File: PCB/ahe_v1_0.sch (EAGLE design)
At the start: 19 parts, among them CN1 1X4-BIG, CN3 1X4SMT, IC1 MS560702BA03-50, IC2 MCP73871-1CCI_ML, IC3 TPS7A2055PDBVR, J1 USB3075-30-A

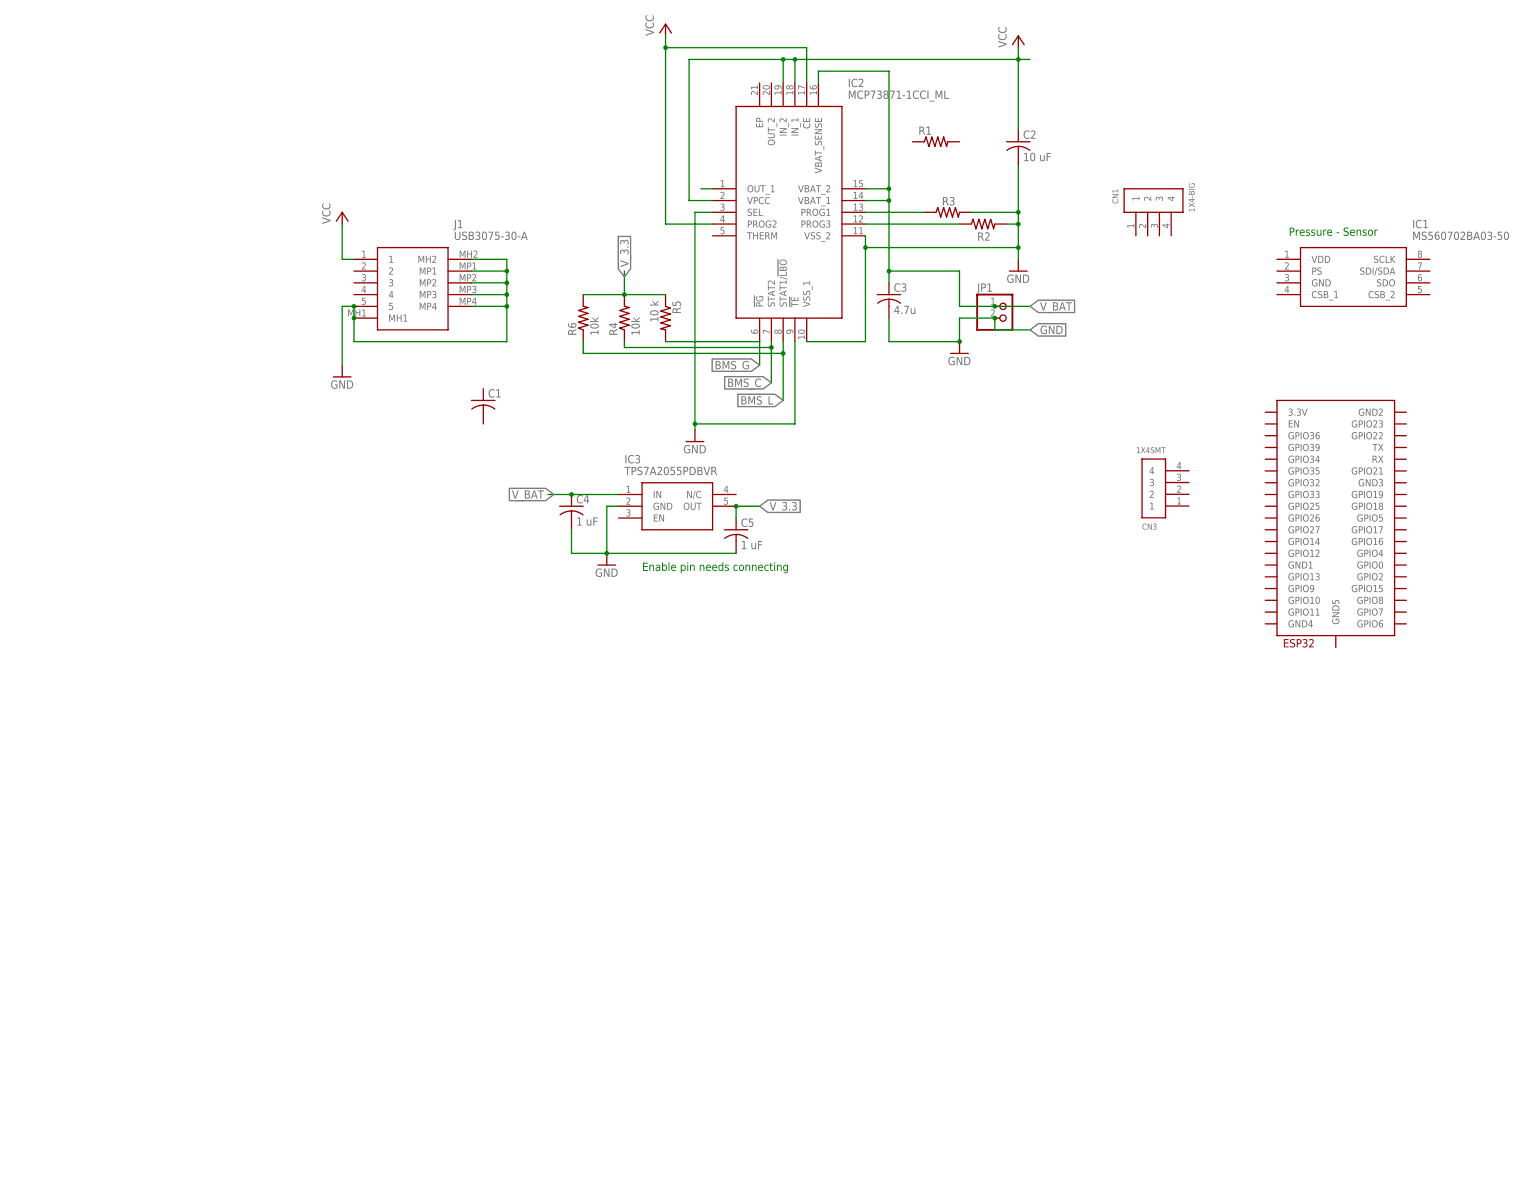
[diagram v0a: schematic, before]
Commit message: Completed BMS/LDO
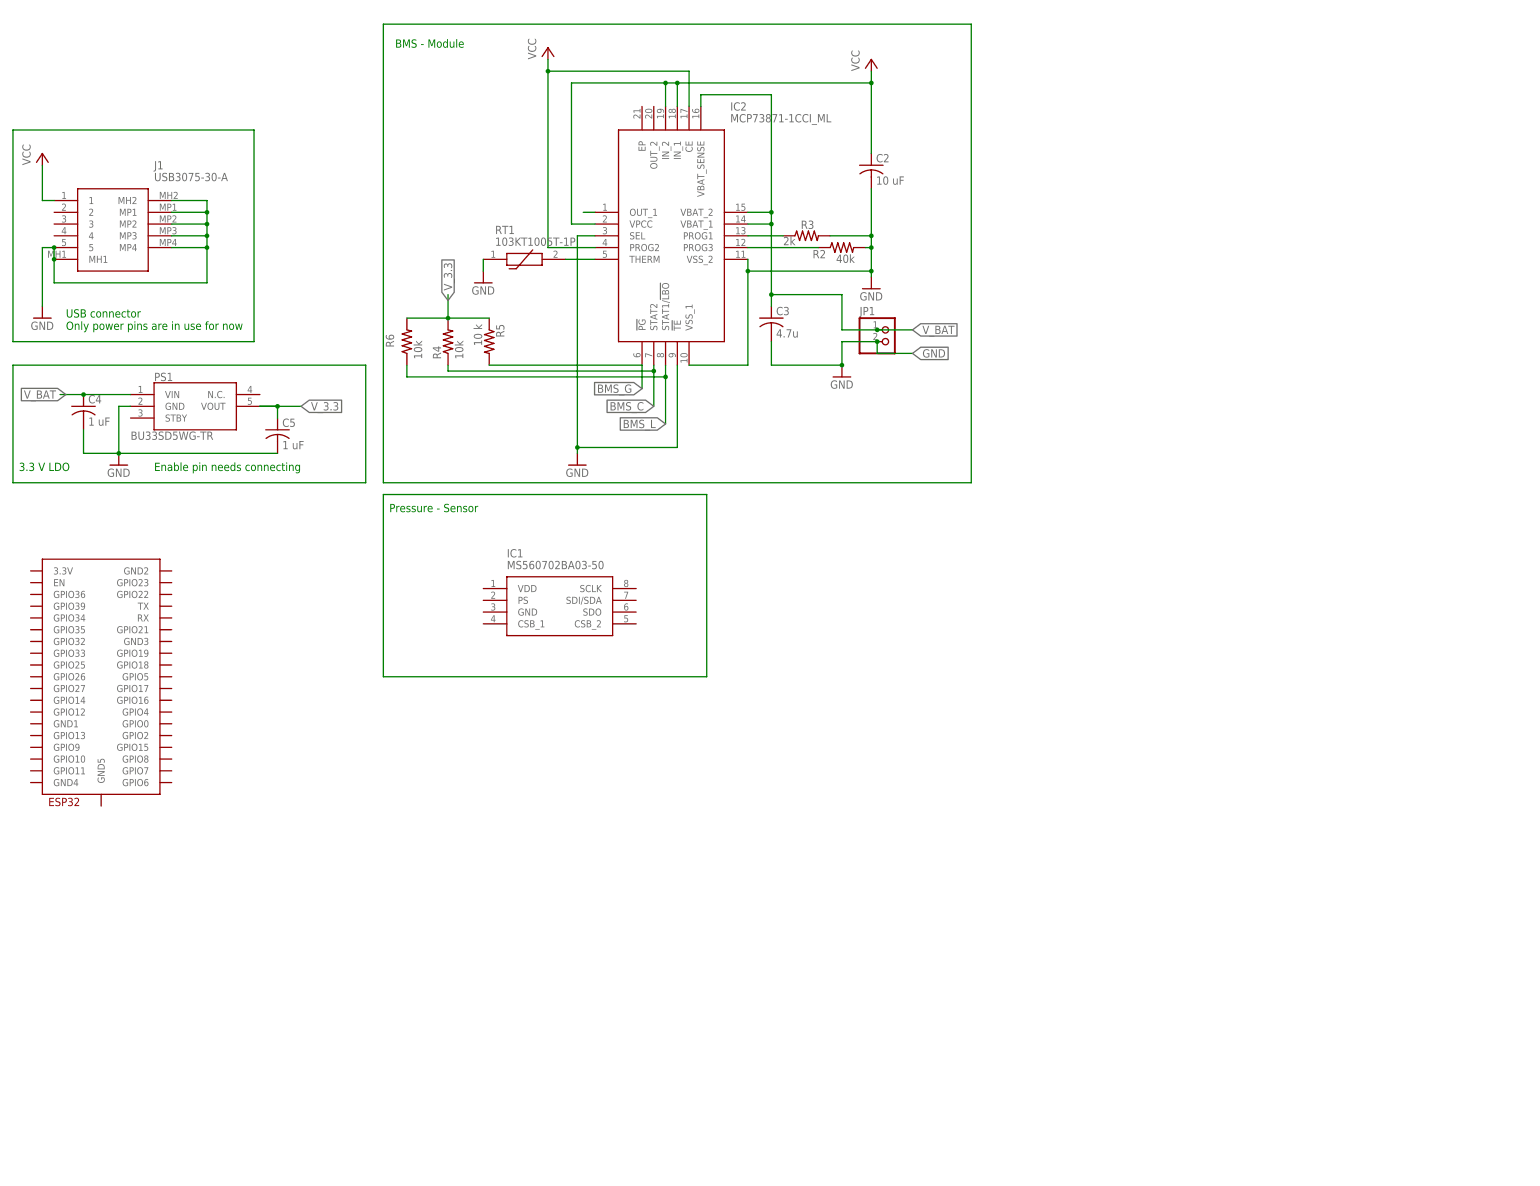
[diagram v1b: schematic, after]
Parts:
- removed C1: (no value), rcl:C-USC0805
- removed CN1: 1X4-BIG, adafruit:1X4-BIG
- removed CN3: 1X4SMT, adafruit:1X4SMT
- removed IC3: TPS7A2055PDBVR, TPS7A2055PDBVR:TPS7A2055PDBVR
- removed R1: (no value), rcl:R-US_R0805
- added PS1: BU33SD5WG-TR, BU33SD5WG-TR:BU33SD5WG-TR
- added RT1: 103KT1005T-1P, 103KT1005T-1P:103KT1005T-1P
- R2: value (none) -> 40k
- R3: value (none) -> 2k
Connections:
- new net N$3: IC2.THERM, RT1.2
- net GND: now also PS1.GND, RT1.1; no longer IC3.GND
- net V_3.3: now also PS1.VOUT; no longer IC3.OUT
- net V_BAT: now also PS1.VIN; no longer IC3.IN
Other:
- note added: "3.3 V LDO"
- note added: "BMS - Module"
- note added: "USB connector Only power pins are in use for now"
- moved on the sheet: C2, C3, C4, C5, IC1, IC2, J1, JP1, R2, R3, R4, R5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

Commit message: #6 pressure sensor completed
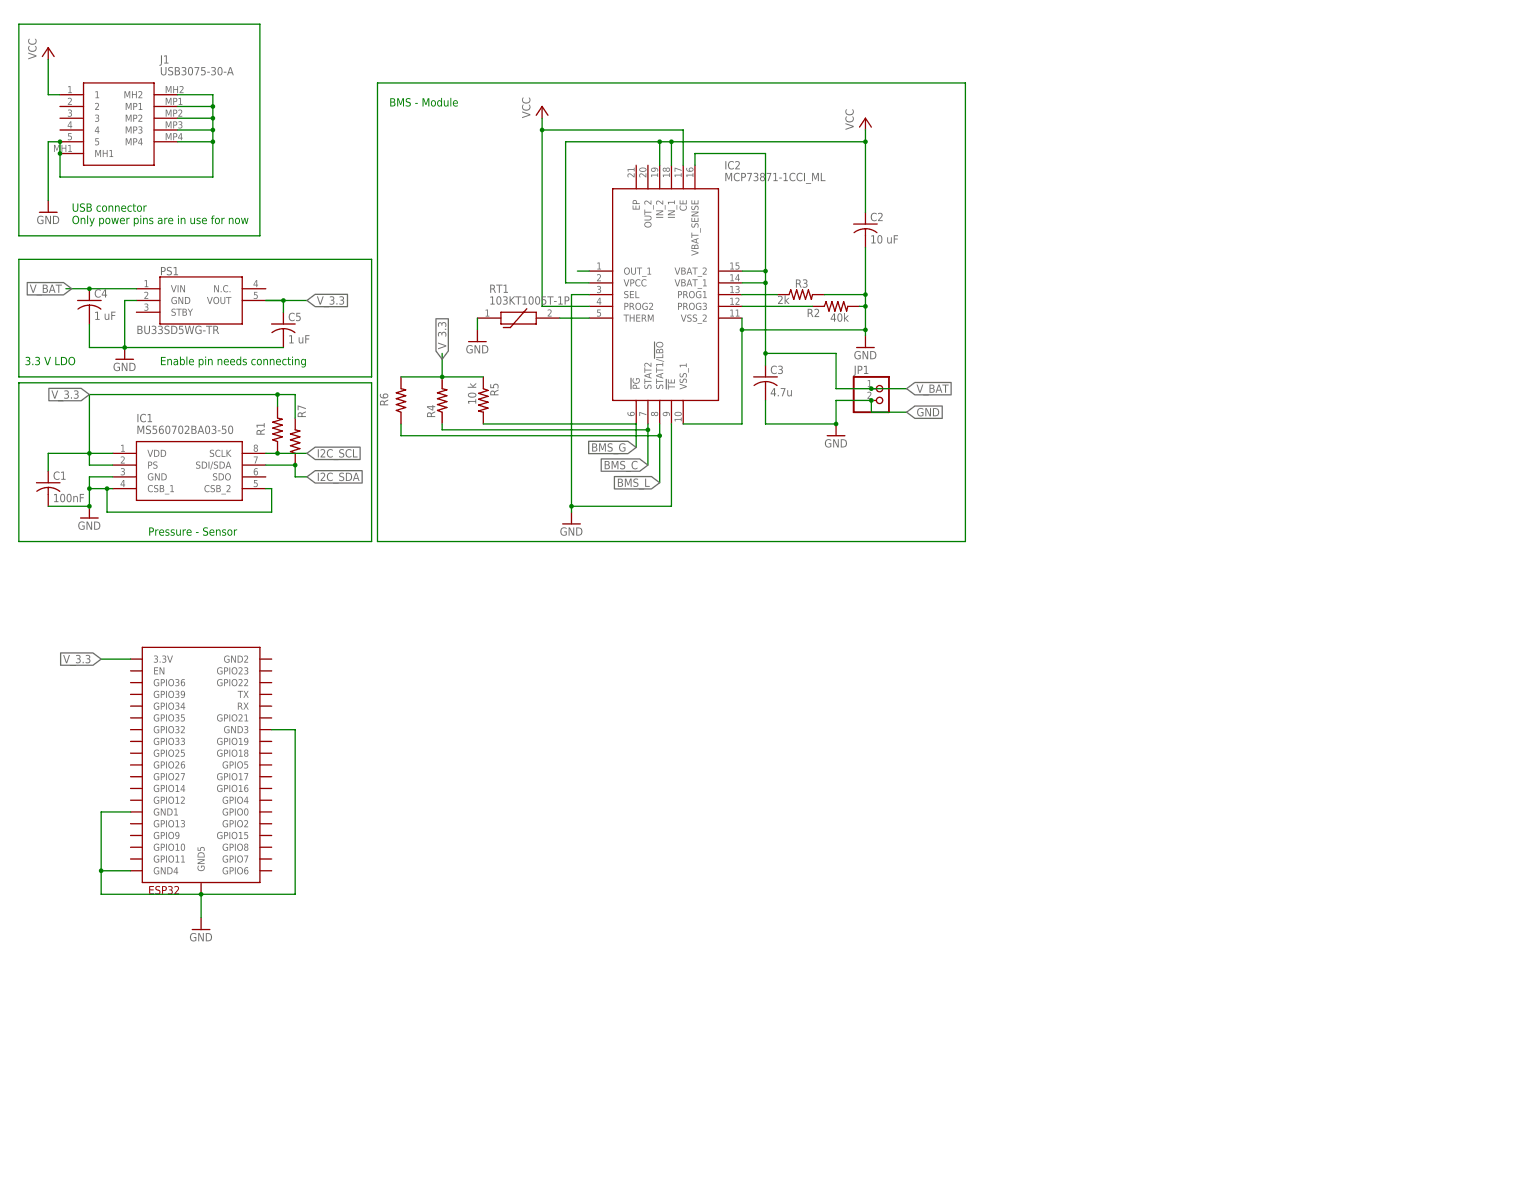
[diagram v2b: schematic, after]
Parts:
- added C1: 100nF, rcl:C-USC0805
- added R1, R7: 10k, rcl:R-US_R0805
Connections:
- new net I2C_SCL: IC1.SCLK, R1.1
- new net I2C_SDA: IC1.SDI/SDA, R7.1
- net GND: now also C1.2, IC1.CSB_1, IC1.CSB_2, IC1.GND, U$1.GND1, U$1.GND3, U$1.GND4, U$1.GND5
- net V_3.3: now also C1.1, IC1.PS, IC1.VDD, R1.2, R7.2, U$1.3.3V
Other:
- moved on the sheet: C2, C3, C4, C5, IC1, IC2, J1, JP1, PS1, R2, R3, R4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

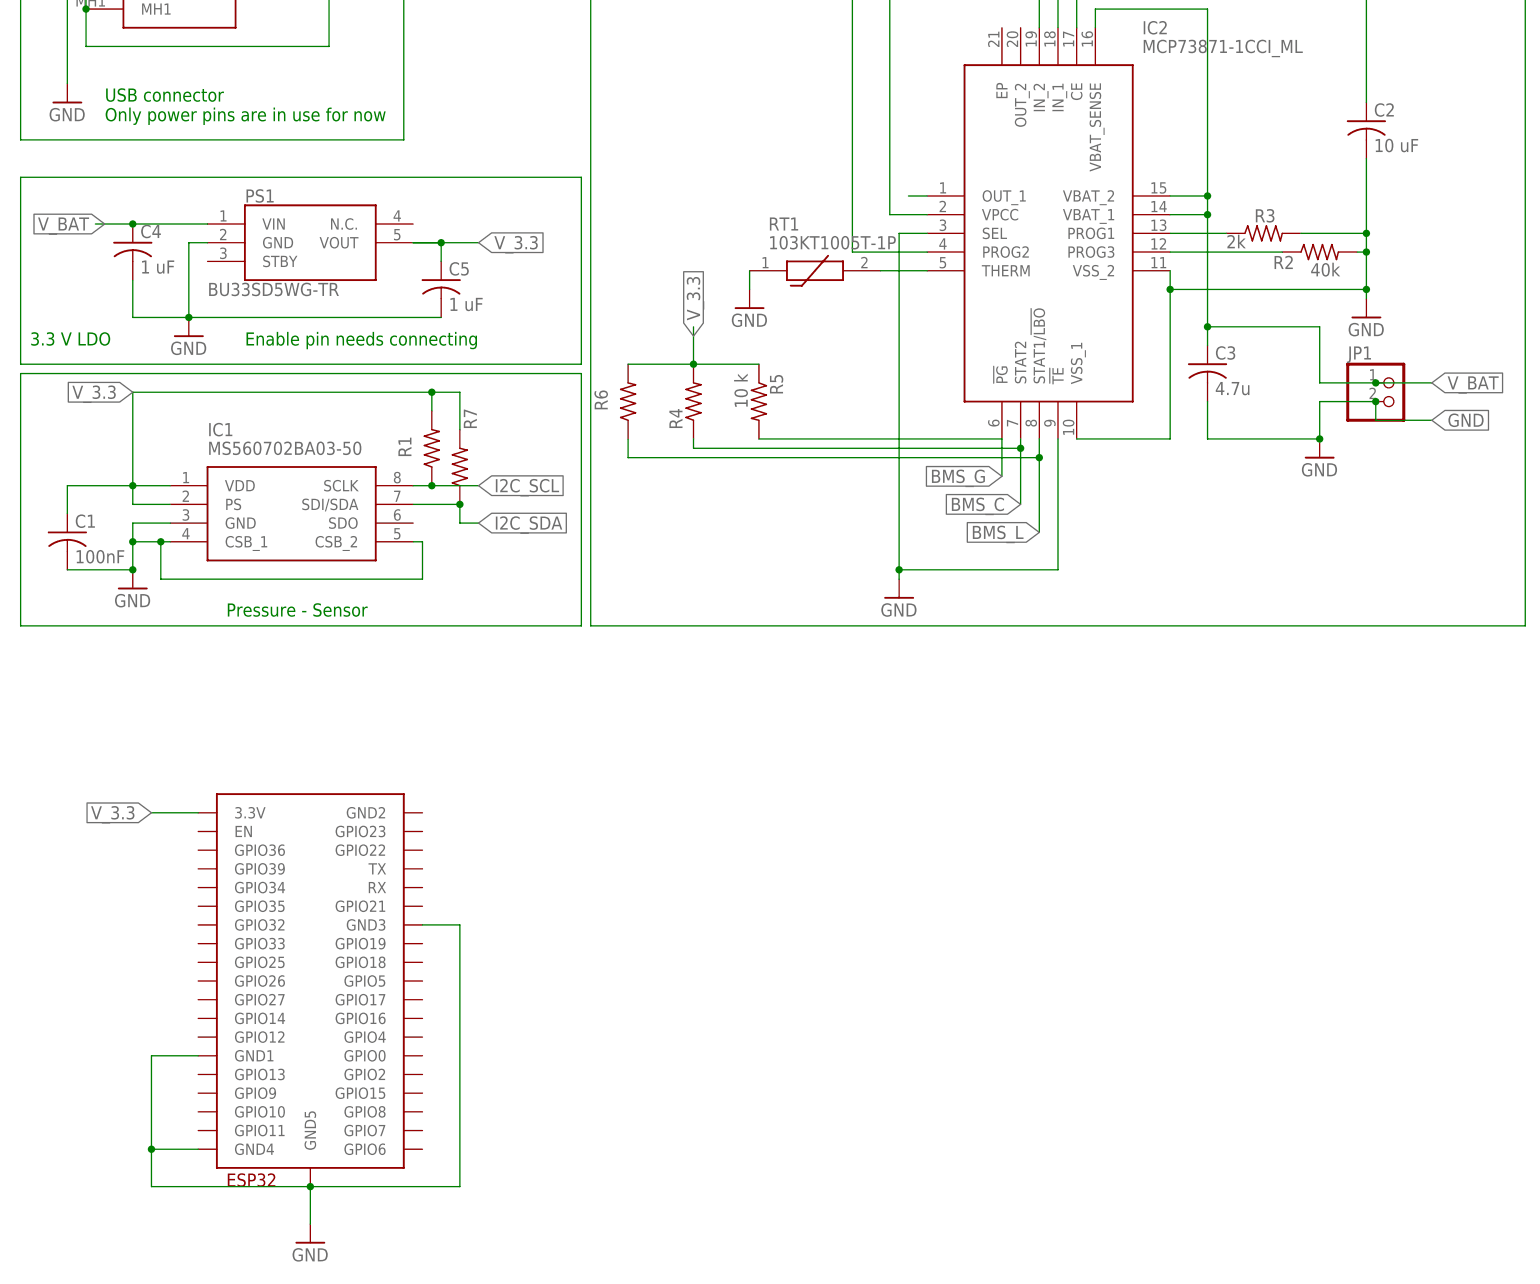
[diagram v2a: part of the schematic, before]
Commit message: updated the ESP32 library to match actual product
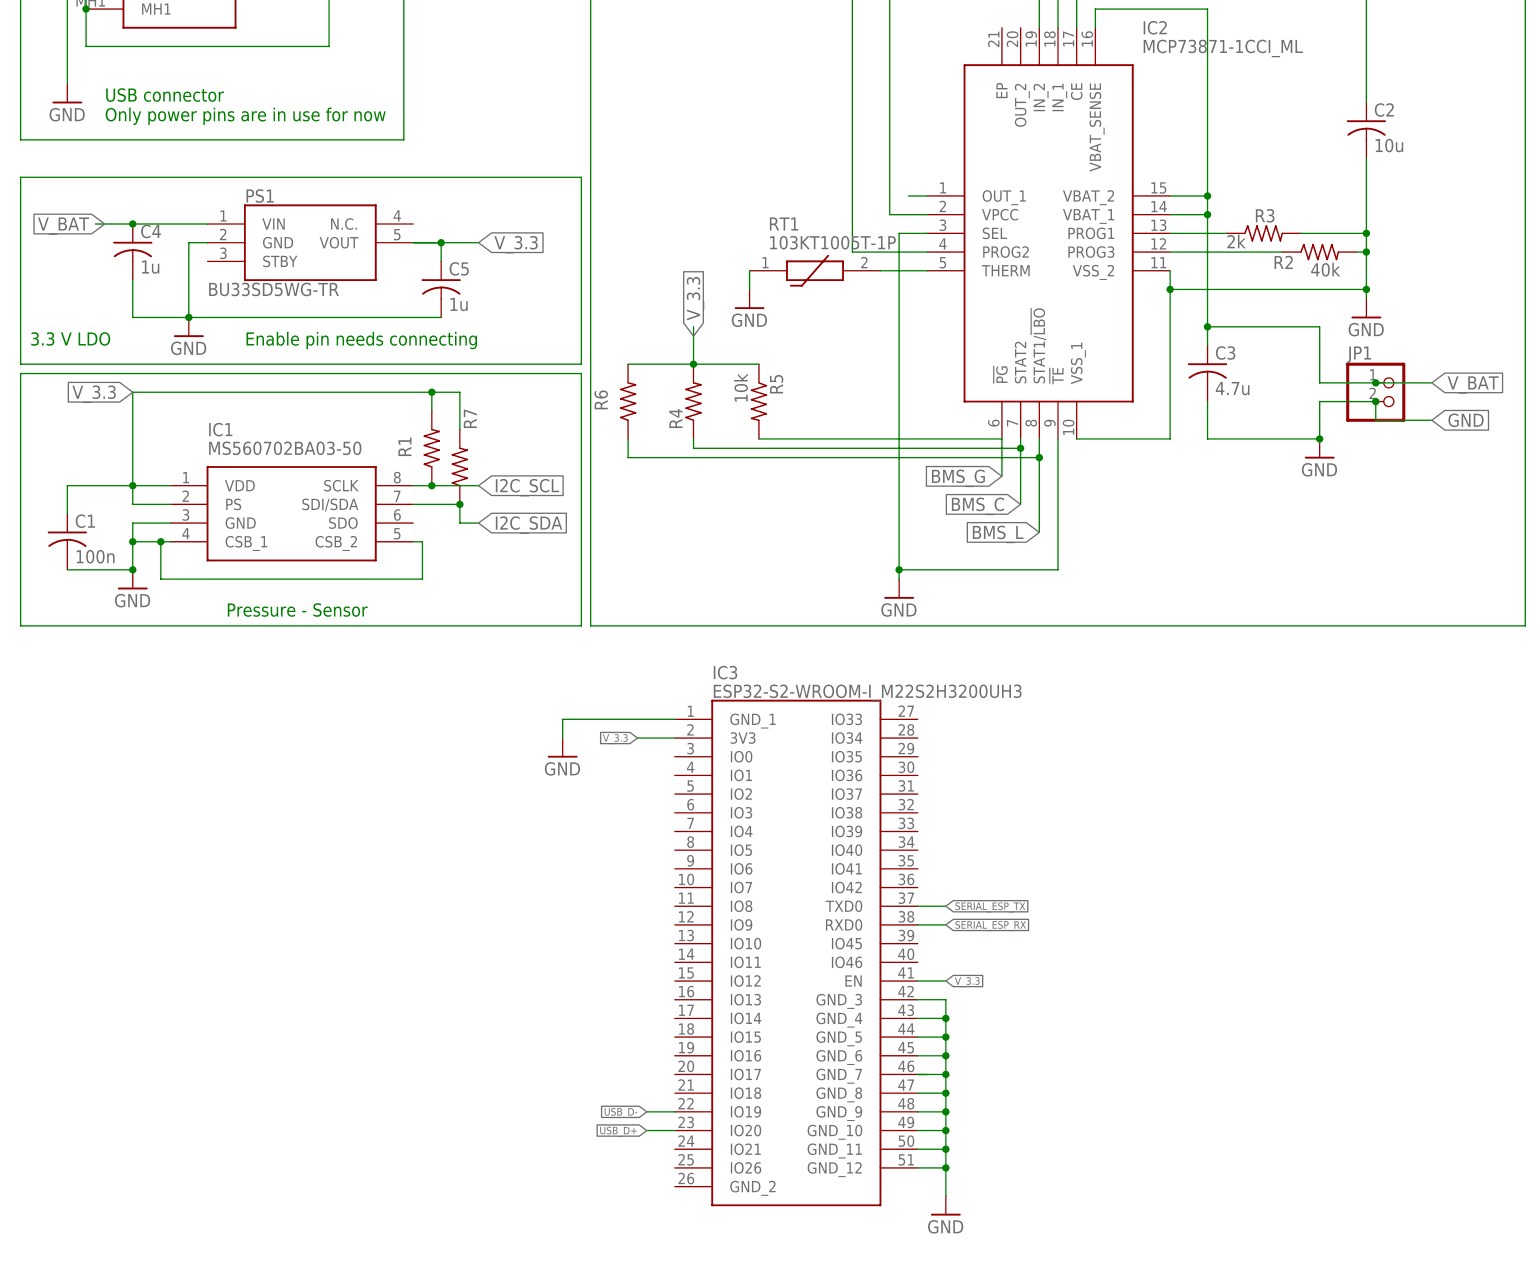
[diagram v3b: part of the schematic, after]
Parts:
- removed U$1: ESP32-WROOM, ESP32:ESP32-WROOM
- added IC3: ESP32-S2-WROOM-I_M22S2H3200UH3, ESP32-S2-WROOM-I_M22S2H3200UH3:ESP32-S2-WROOM-I_M22S2H3200UH3
- C1: value 100nF -> 100n
- C2: value 10 uF -> 10u
- C4, C5: value 1 uF -> 1u
- R5: value 10 k -> 10k
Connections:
- new net SERIAL_ESP_RX: IC3.RXD0
- new net SERIAL_ESP_TX: IC3.TXD0
- new net USB_D+: IC3.IO20
- new net USB_D-: IC3.IO19
- net GND: now also IC3.GND_1, IC3.GND_10, IC3.GND_11, IC3.GND_12, IC3.GND_3, IC3.GND_4, IC3.GND_5, IC3.GND_6, IC3.GND_7, IC3.GND_8, IC3.GND_9; no longer U$1.GND1, U$1.GND3, U$1.GND4, U$1.GND5
- net V_3.3: now also IC3.3V3, IC3.EN; no longer U$1.3.3V
